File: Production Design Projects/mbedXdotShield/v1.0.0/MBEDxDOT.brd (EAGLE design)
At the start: 81.3 x 53.3 mm, 68 parts, among them CON1 47346-0001, CON2 S2B-PH-SM4-TB(LF)(SN), Q1 12MHz, SW2 SKRKAEE010, T1 BSS84, U1 MTXDOT-EU1-A00-1, U2 TLV73333PDBVT, U3 AT45DB321E-SHF-B

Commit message: Final release of V1.0.0
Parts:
- added R27: 0, mbed-HDK-RLCQ:0402
- added SW3: JS202011JCQN, mbed-HDK-Switch:JS202011JCQN
- moved C5 0.34 mm to (53.4, -106.9)
- renumbered SW2 to GPIO1
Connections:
- new net N$49: BRD1.2, BRD1.4, R27.1
- new net N$50: R17.2, SW3.6
- new net N$51: R18.2, SW3.2
- net +3.3V_TGT: now also R27.2; no longer BRD1.2, BRD1.4
- net UART1_RX: now also SW3.3, SW3.5; no longer R17.2
- net UART1_TX: now also SW3.1, SW3.7; no longer R18.2
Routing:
- net GND: track 19.2 -> 77.6 mm
- net +3.3V_TGT: track 46.5 -> 94.0 mm
- net UART1_TX: track 72.9 -> 95.1 mm, vias 3 -> 4
- net UART1_RX: track 69.7 -> 88.6 mm, vias 3 -> 2
- net N$51: track 0.00 -> 16.3 mm, vias 0 -> 1
- net N$50: track 0.00 -> 12.1 mm, vias 0 -> 1
- net N$49: track 0.00 -> 11.8 mm
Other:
- board text added: "OFF ON"
- board text added: "XDOT MCU FLASH MEMORY UART SWAP LORA ANTENNA"
- board text added: "mbed-xDOT-shield v1.0.0"
- board text removed: "XDOT MCU FLASH MEMORY LORA ANTENNA"
- board text removed: "mbed-xDOT v1.0.0"

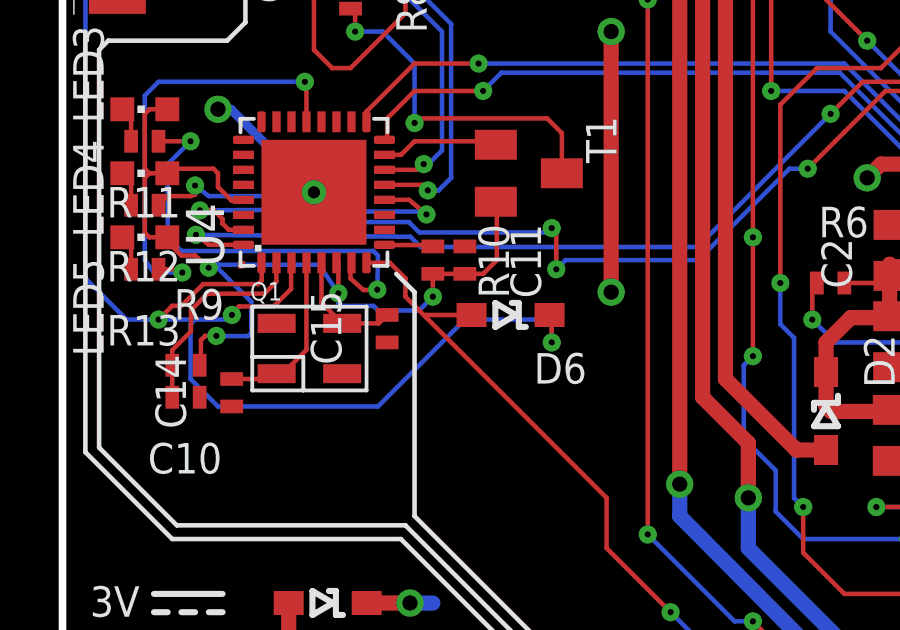
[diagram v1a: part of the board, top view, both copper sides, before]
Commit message: Change part to D6 to BAT60J
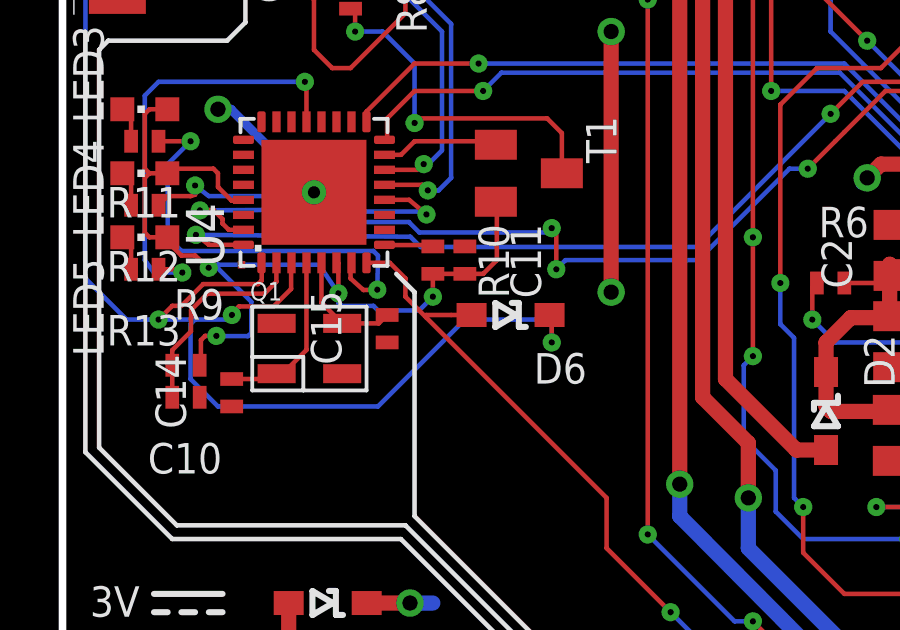
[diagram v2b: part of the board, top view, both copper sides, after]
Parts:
- D6: value BAT60A -> BAT60J
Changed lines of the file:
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@@
 <attribute name="MFN" value="BAT60AE6327HTSA1" x="7.9248" y="-123.5964" size="1.778" layer="27" rot="R180" display="off"/>
-</element>
-<element name="D6" library="mbed-HDK-Transistor" package="SOD323" value="BAT60A" x="14.0208" y="-113.9952" rot="R180">
-<attribute name="OC-DIGIKEY" value="BAT60AE6327HTSA1CT-ND" x="14.0208" y="-113.9952" size="1.778" layer="27" rot="R180" display="off"/>
-<attribute name="MFN" value="BAT60AE6327HTSA1" x="14.0208" y="-113.9952" size="1.778" layer="27" rot="R180" display="off"/>
-<attribute name="OC-NEWARK" value="85X4127" x="14.0208" y="-113.9952" size="1.778" layer="27" rot="R180" display="off"/>
-<attribute name="OC-MOUSER" value="726-BAT60AE6327" x="14.0208" y="-113.9952" size="1.778" layer="27" rot="R180" display="off"/>
-<attribute name="MF" value="Infineon" x="14.0208" y="-113.9952" size="1.778" layer="27" rot="R180" display="off"/>
 </element>
 <element name="C16" library="mbed-HDK-RLCQ" package="0603" value="10uF" x="9.906" y="-94.7928"/>
@@
 <attribute name="OC-NEWARK" value="" x="53.0352" y="-99.3648" size="1.778" layer="27" rot="R90" display="off"/>
 <attribute name="OC-MOUSER" value="611-JS202011JCQN" x="53.0352" y="-99.3648" size="1.778" layer="27" rot="R90" display="off"/>
+</element>
+<element name="D6" library="mbed-HDK-Transistor" package="SOD323" value="BAT60J" x="14.0208" y="-113.9952" rot="R180">
+<attribute name="OC-DIGIKEY" value="497-3707-6-ND" x="14.0208" y="-113.9952" size="1.778" layer="27" rot="R180" display="off"/>
+<attribute name="OC-MOUSER" value="511-BAT60JFILM" x="14.0208" y="-113.9952" size="1.778" layer="27" rot="R180" display="off"/>
+<attribute name="MFN" value="BAT60JFILM" x="14.0208" y="-113.9952" size="1.778" layer="27" rot="R180" display="off"/>
+<attribute name="MF" value="STMicroelectronics" x="14.0208" y="-113.9952" size="1.778" layer="27" rot="R180" display="off"/>
+<attribute name="OC-NEWARK" value="89K1218" x="14.0208" y="-113.9952" size="1.778" layer="27" rot="R180" display="off"/>
 </element>
 </elements>
@@
 <wire x1="19.3548" y1="-123.9012" x2="20.574" y2="-125.1204" width="0.1524" layer="16"/>
 <wire x1="20.574" y1="-125.1204" x2="22.2504" y2="-125.1204" width="0.1524" layer="16"/>
+<wire x1="12.0396" y1="-113.9952" x2="11.2014" y2="-113.9952" width="0.1524" layer="1"/>
+<wire x1="11.2014" y1="-113.9952" x2="11.2014" y2="-114.0714" width="0.1524" layer="1"/>
 <contactref element="D6" pad="A"/>
-<wire x1="12.7208" y1="-113.9952" x2="11.2014" y2="-113.9952" width="0.1524" layer="1"/>
-<wire x1="11.2014" y1="-113.9952" x2="11.2014" y2="-114.0714" width="0.1524" layer="1"/>
+<wire x1="12.7208" y1="-113.9952" x2="12.0396" y2="-113.9952" width="0.1524" layer="1"/>
+<wire x1="12.7208" y1="-113.9952" x2="12.8016" y2="-113.9952" width="0.1524" layer="1"/>
 </signal>
 <signal name="WAKE">
@@
 <wire x1="7.62" y1="-93.8784" x2="7.62" y2="-92.007" width="0.1524" layer="1"/>
 <wire x1="7.62" y1="-92.007" x2="7.053" y2="-91.44" width="0.1524" layer="1"/>
-<contactref element="D6" pad="K"/>
-<wire x1="15.3208" y1="-113.9952" x2="15.3924" y2="-113.9952" width="0.1524" layer="1"/>
-<wire x1="15.3924" y1="-113.9952" x2="15.3924" y2="-114.9096" width="0.1524" layer="1"/>
 <via x="15.3924" y="-114.9096" extent="1-16" drill="0.2032"/>
 <wire x1="15.3924" y1="-114.9096" x2="15.3924" y2="-114.1476" width="0.1524" layer="16"/>
@@
 <wire x1="3.3528" y1="-116.1288" x2="3.3528" y2="-114.3" width="0.1524" layer="16"/>
 <wire x1="3.3528" y1="-114.3" x2="3.5052" y2="-114.1476" width="0.1524" layer="16"/>
+<contactref element="D6" pad="K"/>
+<wire x1="15.3208" y1="-113.9952" x2="15.3924" y2="-113.9952" width="0.1524" layer="1"/>
+<wire x1="15.3924" y1="-113.9952" x2="15.3924" y2="-114.9096" width="0.1524" layer="1"/>
 </signal>
 <signal name="+3.3V_IF">
